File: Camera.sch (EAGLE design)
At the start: 53 parts, among them SW5 THAU13-AB-R, SW6 THAU13-AB-R, SW7 TVAF06-A020B-R, SW8 TVAF06-A020B-R, U4 OPA340N, U5 DRIVER-LV8548MC-AH(SOIC10), U6 I-02247_NJM2845

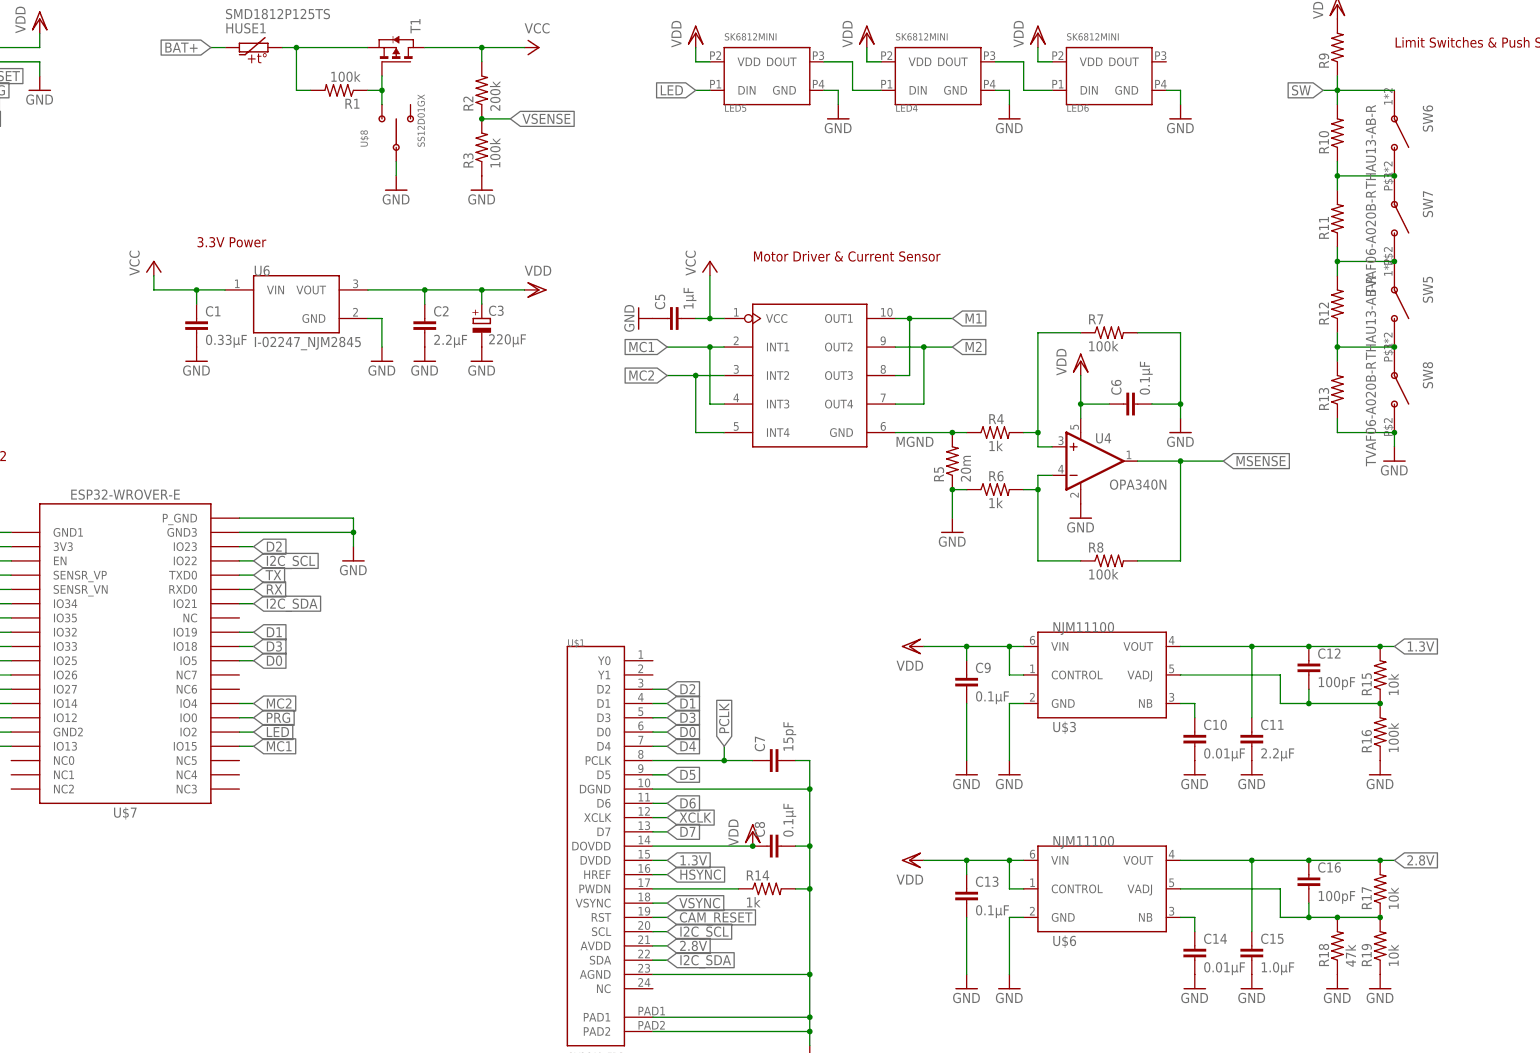
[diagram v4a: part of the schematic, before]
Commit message: Format silk
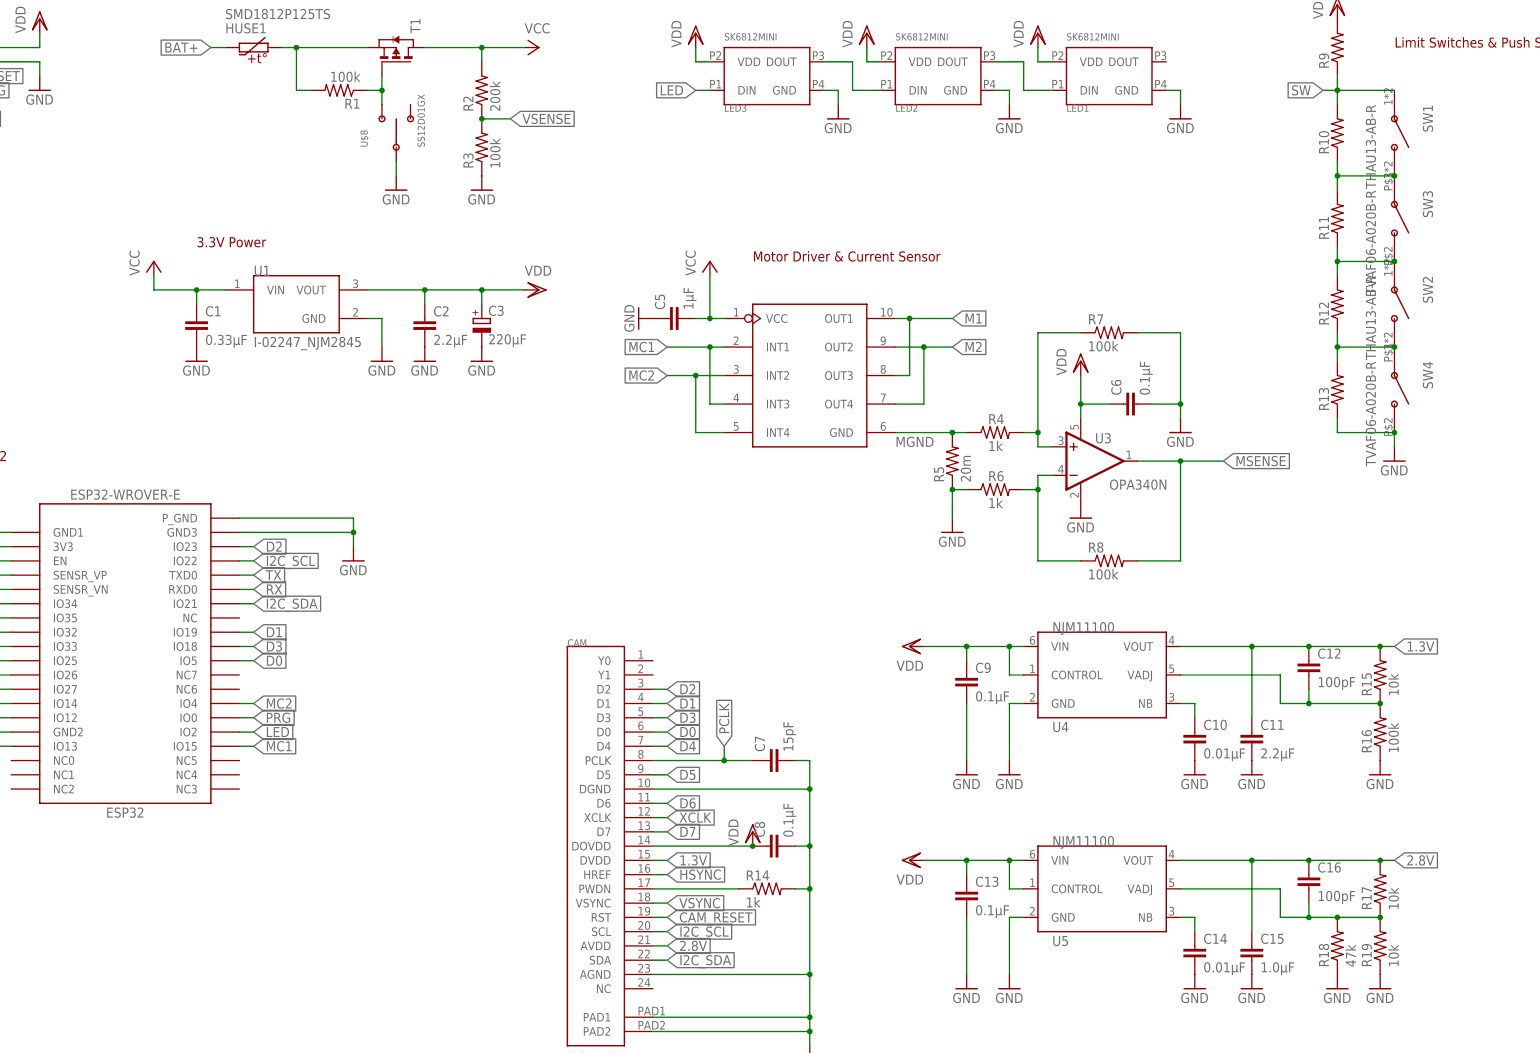
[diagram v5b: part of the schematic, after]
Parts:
- removed U$3, U$6: NJM11100, regulators:NJM11100
- added U2: DRIVER-LV8548MC-AH(SOIC10), DRIVER-LV8548MC-AH_SOIC10_:DRIVER-LV8548MC-AH(SOIC10)
- added U3: OPA340N, burr-brown:OPA340N
- U4: value OPA340N -> NJM11100; device burr-brown:OPA340N -> regulators:NJM11100
- U5: value DRIVER-LV8548MC-AH(SOIC10) -> NJM11100; device DRIVER-LV8548MC-AH_SOIC10_:DRIVER-LV8548MC-AH(SOIC10) -> regulators:NJM11100
- renumbered LED4 to LED2, LED5 to LED3, LED6 to LED1, SW5 to SW2, SW6 to SW1, SW7 to SW3, SW8 to SW4, U$1 to CAM, U$7 to ESP32, U6 to U1
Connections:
- net 1.3V: now also U4.VOUT; no longer U$3.VOUT
- net 2.8V: now also U5.VOUT; no longer U$6.VOUT
- net GND: now also U3.V-, U4.GND, U5.GND; no longer U$3.GND, U$6.GND, U4.V-
- net M1: now also U2.OUT1, U2.OUT3; no longer U5.OUT1, U5.OUT3
- net M2: now also U2.OUT2, U2.OUT4; no longer U5.OUT2, U5.OUT4
- net MC1: now also U2.INT1, U2.INT3; no longer U5.INT1, U5.INT3
- net MC2: now also U2.INT2, U2.INT4; no longer U5.INT2, U5.INT4
- net MGND: now also U2.GND; no longer U5.GND
- net MSENSE: now also U3.OUT; no longer U4.OUT
- net N$1: now also U4.NB; no longer U$3.NB
- net N$15: now also U3.-IN; no longer U4.-IN
- net N$16: now also U3.+IN; no longer U4.+IN
- net N$2: now also U4.VADJ; no longer U$3.VADJ
- net N$3: now also U5.NB; no longer U$6.NB
- net N$4: now also U5.VADJ; no longer U$6.VADJ
- net VCC: now also U2.VCC; no longer U5.VCC
- net VDD: now also U3.V+, U4.CONTROL, U4.VIN, U5.CONTROL, U5.VIN; no longer U$3.CONTROL, U$3.VIN, U$6.CONTROL, U$6.VIN, U4.V+
